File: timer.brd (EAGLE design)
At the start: 100 x 100 mm, 58 parts, among them IC1 CD4060, IC2 7805TV, K1 ZF112

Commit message: Added Values
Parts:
- C1: value (none) -> 100uF/16V
- C2: value (none) -> 0.3uF
- C3: value (none) -> 0.1uF
- C4: value (none) -> 100nF
- C5: value (none) -> 0.22uF
- JP1: value (none) -> 9V Battery
- JP2: value (none) -> Relay
- K1: value ZF112 -> 5V
- R1, R11, R20: value (none) -> 1K
- R12: value (none) -> 100K
- R15: value (none) -> 1M
- R16, R18: value (none) -> 10M
- R17: value (none) -> 22M
- R19: value (none) -> 3K
- S1: value DPDT_SEC -> DPDT Slide Switch
- S2: value MOMENTARY-SWITCH-SPST-PTH-6.0MM -> SPST Momentary Switch 6mm
- S3: value (none) -> DIP Switch
- S4: value (none) -> SPDT
- T1: value (none) -> BC547

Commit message: Values + OS Logo + Titlesheet
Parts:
- added LOGO1: OSHW-LOGOS-COPPER, SparkFun-Aesthetics:OSHW-LOGO-S_COPPER
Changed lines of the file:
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@@
 <layer number="112" name="tSilk" color="7" fill="1" visible="yes" active="yes"/>
 <layer number="113" name="IDFDebug" color="4" fill="1" visible="yes" active="yes"/>
+<layer number="114" name="Badge_Outline" color="7" fill="1" visible="no" active="yes"/>
+<layer number="115" name="ReferenceISLANDS" color="7" fill="1" visible="no" active="yes"/>
 <layer number="116" name="Patch_BOT" color="9" fill="4" visible="yes" active="yes"/>
 <layer number="118" name="Rect_Pads" color="7" fill="1" visible="yes" active="yes"/>
@@
 <attribute name="VALUE" x="73.75" y="78.722" size="1.27" layer="27" ratio="10" rot="R180"/>
 </element>
+<element name="LOGO1" library="SparkFun-Aesthetics" library_urn="urn:adsk.eagle:library:507" package="OSHW-LOGO-S_COPPER" value="OSHW-LOGOS-COPPER" x="119" y="15" smashed="yes"/>
 </elements>
 <signals>

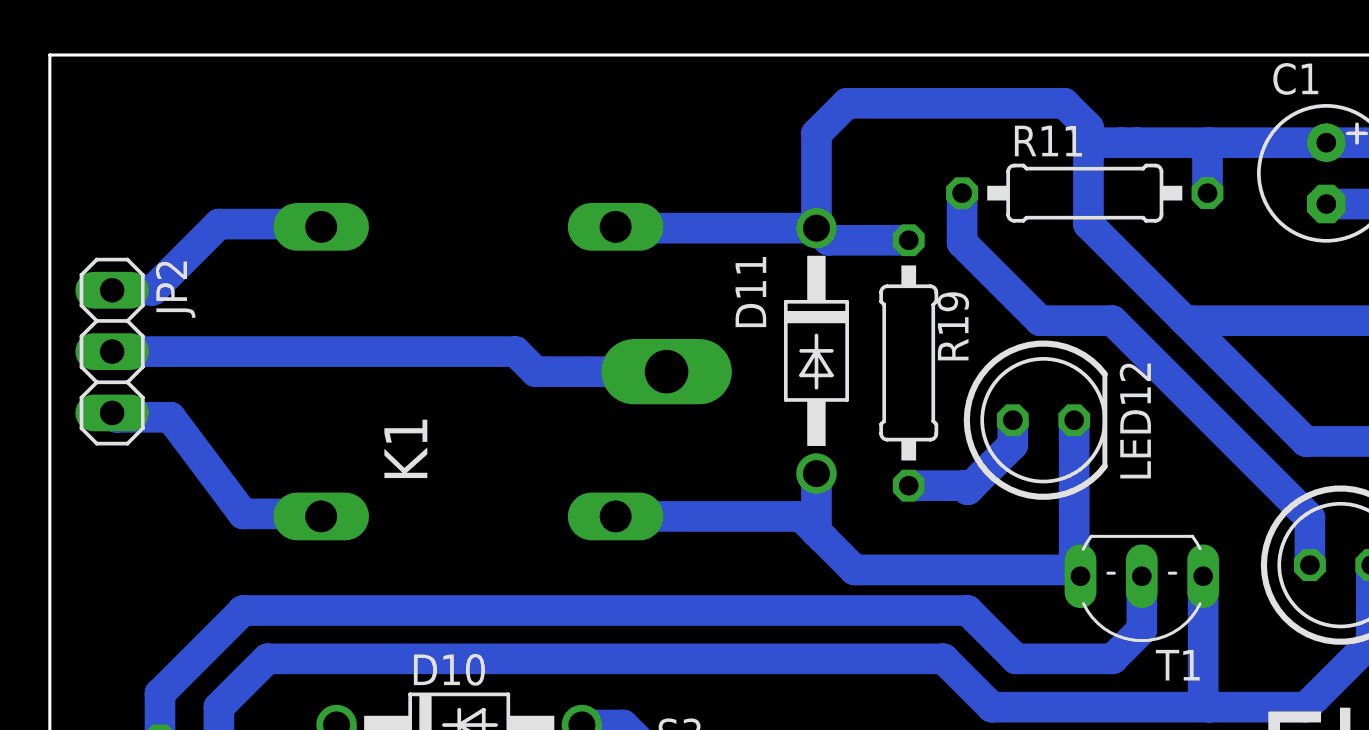
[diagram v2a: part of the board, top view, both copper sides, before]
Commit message: Changed Relay Output Connector
Pinhead JP2 changed to screw terminal J1
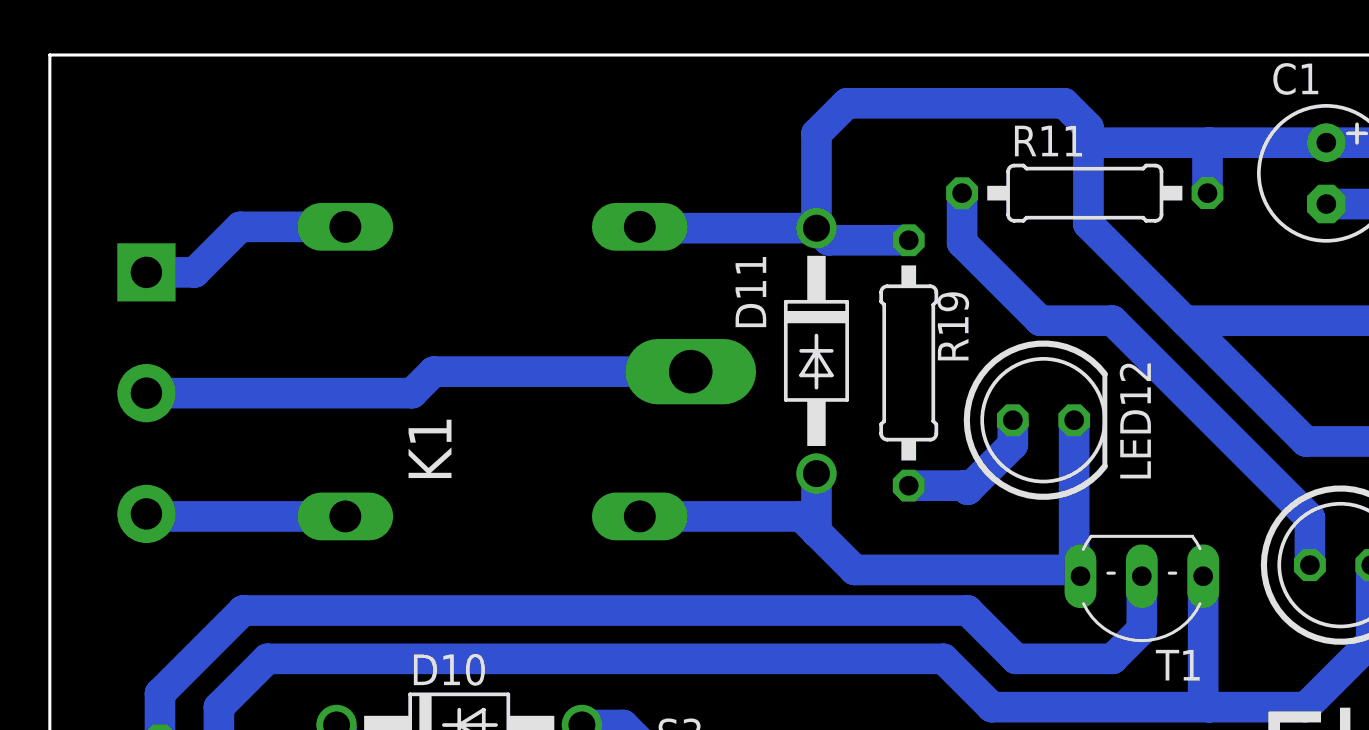
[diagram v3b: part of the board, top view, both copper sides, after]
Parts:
- removed JP2: Relay, pinhead:1X03
- added J1: Relay, SparkFun-Connectors:SCREWTERMINAL-5MM-3
- moved K1 1.00 mm to (44.3, 83.9)
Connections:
- net N$48: now also J1.2; no longer JP2.2
- net N$49: now also J1.3; no longer JP2.3
- net N$50: now also J1.1; no longer JP2.1
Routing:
- net N$49: track 10.8 -> 8.42 mm
- net N$45: track 28.9 -> 27.9 mm
- net 5V: track 140.5 -> 139.5 mm
- net N$50: track 9.84 -> 9.18 mm
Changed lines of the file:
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@@
 <layer number="230" name="230bmp" color="7" fill="1" visible="yes" active="yes"/>
 <layer number="231" name="231bmp" color="7" fill="1" visible="yes" active="yes"/>
+<layer number="232" name="Eagle3D_PG2" color="7" fill="1" visible="yes" active="yes"/>
+<layer number="233" name="Eagle3D_PG3" color="7" fill="1" visible="yes" active="yes"/>
 <layer number="248" name="Housing" color="7" fill="1" visible="yes" active="yes"/>
 <layer number="249" name="Edge" color="7" fill="1" visible="yes" active="yes"/>
@@
 <attribute name="VALUE" x="119.405" y="89.88" size="1.27" layer="27" rot="R270"/>
 </element>
-<element name="JP2" library="pinhead" library_urn="urn:adsk.eagle:library:325" package="1X03" package3d_urn="urn:adsk.eagle:package:22458/2" value="Relay" x="28.58" y="84.72" smashed="yes" rot="R270">
-<attribute name="NAME" x="30.4088" y="88.6062" size="1.27" layer="25" ratio="10" rot="R270"/>
-<attribute name="VALUE" x="30.405" y="84.53" size="1.27" layer="27" rot="R270"/>
-</element>
-<element name="K1" library="relay" library_urn="urn:adsk.eagle:library:339" package="ZF112" package3d_urn="urn:adsk.eagle:package:24315/1" value="5V" x="43.33" y="83.89" smashed="yes" rot="MR0">
-<attribute name="MF" value="" x="16.66" y="75" size="1.778" layer="28" rot="MR0" display="off"/>
-<attribute name="MPN" value="" x="16.66" y="75" size="1.778" layer="28" rot="MR0" display="off"/>
-<attribute name="NAME" x="41.63" y="79.27" size="1.778" layer="25" ratio="10" rot="R90"/>
-<attribute name="OC_FARNELL" value="unknown" x="16.66" y="75" size="1.778" layer="28" rot="MR0" display="off"/>
-<attribute name="OC_NEWARK" value="unknown" x="16.66" y="75" size="1.778" layer="28" rot="MR0" display="off"/>
+<element name="K1" library="relay" library_urn="urn:adsk.eagle:library:339" package="ZF112" package3d_urn="urn:adsk.eagle:package:24315/1" value="5V" x="44.33" y="83.89" smashed="yes" rot="MR0">
+<attribute name="MF" value="" x="17.66" y="75" size="1.778" layer="28" rot="MR0" display="off"/>
+<attribute name="MPN" value="" x="17.66" y="75" size="1.778" layer="28" rot="MR0" display="off"/>
+<attribute name="NAME" x="42.63" y="79.27" size="1.778" layer="25" ratio="10" rot="R90"/>
+<attribute name="OC_FARNELL" value="unknown" x="17.66" y="75" size="1.778" layer="28" rot="MR0" display="off"/>
+<attribute name="OC_NEWARK" value="unknown" x="17.66" y="75" size="1.778" layer="28" rot="MR0" display="off"/>
 </element>
 <element name="LED1" library="led" library_urn="urn:adsk.eagle:library:259" package="LED5MM" package3d_urn="urn:adsk.eagle:package:15799/2" value="" x="113.12" y="2.26" smashed="yes" rot="R270">
@@
 </element>
 <element name="LOGO1" library="SparkFun-Aesthetics" library_urn="urn:adsk.eagle:library:507" package="OSHW-LOGO-S_COPPER" value="OSHW-LOGOS-COPPER" x="119" y="15" smashed="yes"/>
+<element name="J1" library="SparkFun-Connectors" library_urn="urn:adsk.eagle:library:513" package="SCREWTERMINAL-5MM-3" value="Relay" x="30" y="88" smashed="yes" rot="MR270">
+<attribute name="NAME" x="27.206" y="84.317" size="0.6096" layer="26" font="vector" ratio="20" rot="MR270"/>
+<attribute name="PROD_ID" value="CONN-10134" x="30" y="88" size="1.778" layer="28" rot="MR270" display="off"/>
+<attribute name="SF_SKU" value="PRT-08433" x="30" y="88" size="1.778" layer="28" rot="MR270" display="off"/>
+<attribute name="VALUE" x="28.095" y="84.571" size="0.6096" layer="28" font="vector" ratio="20" rot="MR270"/>
+</element>
 </elements>
 <signals>
@@
 <contactref element="C4" pad="1"/>
 <wire x1="78.85" y1="93.37" x2="74" y2="93.37" width="1.27" layer="16"/>
-<wire x1="74" y1="93.37" x2="71" y2="93.37" width="1.27" layer="16"/>
-<wire x1="71" y1="93.37" x2="70.37" y2="93.37" width="1.27" layer="16"/>
+<wire x1="74" y1="93.37" x2="69.37" y2="93.37" width="1.27" layer="16"/>
 <wire x1="69" y1="90" x2="73" y2="86" width="1.27" layer="16"/>
 <wire x1="73" y1="86" x2="87" y2="86" width="1.27" layer="16"/>
@@
 <wire x1="61.56" y1="89.33" x2="58.24" y2="89.33" width="1.27" layer="16"/>
 <wire x1="58.24" y1="89.33" x2="57.74" y2="89.83" width="1.27" layer="16"/>
-<wire x1="57.74" y1="89.83" x2="49.4804" y2="89.83" width="1.27" layer="16"/>
-<wire x1="49.4804" y1="89.83" x2="49.426" y2="89.8844" width="1.27" layer="16"/>
+<wire x1="57.74" y1="89.83" x2="50.4804" y2="89.83" width="1.27" layer="16"/>
+<wire x1="50.4804" y1="89.83" x2="50.426" y2="89.8844" width="1.27" layer="16"/>
 <wire x1="57.74" y1="89.83" x2="57.74" y2="93.74" width="1.27" layer="16"/>
 <wire x1="57.74" y1="93.74" x2="59" y2="95" width="1.27" layer="16"/>
@@
 <wire x1="69" y1="93" x2="69" y2="90" width="1.27" layer="16"/>
 <wire x1="59" y1="95" x2="68" y2="95" width="1.27" layer="16"/>
-<wire x1="70.37" y1="93.37" x2="69.37" y2="93.37" width="1.27" layer="16"/>
 <wire x1="69.37" y1="93.37" x2="69" y2="93" width="1.27" layer="16"/>
 </signal>
@@
 <contactref element="D11" pad="A"/>
 <contactref element="K1" pad="2"/>
-<wire x1="49.426" y1="77.8956" x2="57.1044" y2="77.8956" width="1.27" layer="16"/>
+<wire x1="50.426" y1="77.8956" x2="57.1044" y2="77.8956" width="1.27" layer="16"/>
 <wire x1="57.1044" y1="77.8956" x2="57.74" y2="77.26" width="1.27" layer="16"/>
 <wire x1="57.74" y1="79.67" x2="57.74" y2="77.26" width="1.27" layer="16"/>
-<wire x1="57.74" y1="77.26" x2="58" y2="77" width="1.27" layer="16"/>
 <wire x1="68.41" y1="81.88" x2="68.41" y2="75.68" width="1.27" layer="16"/>
 <wire x1="68.41" y1="75.68" x2="68.67" y2="75.42" width="1.27" layer="16"/>
-<wire x1="58" y1="77" x2="59.32" y2="75.68" width="1.27" layer="16"/>
+<wire x1="57.74" y1="77.26" x2="59.32" y2="75.68" width="1.27" layer="16"/>
 <wire x1="59.32" y1="75.68" x2="68.41" y2="75.68" width="1.27" layer="16"/>
 </signal>
@@
 <signal name="N$48">
 <contactref element="K1" pad="P"/>
-<contactref element="JP2" pad="2"/>
-<wire x1="28.58" y1="84.72" x2="45.28" y2="84.72" width="1.27" layer="16"/>
-<wire x1="46.11" y1="83.89" x2="51.5342" y2="83.89" width="1.27" layer="16"/>
-<wire x1="45.28" y1="84.72" x2="46.11" y2="83.89" width="1.27" layer="16"/>
+<contactref element="J1" pad="2"/>
+<wire x1="52.5342" y1="83.89" x2="41.89" y2="83.89" width="1.27" layer="16"/>
+<wire x1="41.89" y1="83.89" x2="41" y2="83" width="1.27" layer="16"/>
+<wire x1="41" y1="83" x2="30" y2="83" width="1.27" layer="16"/>
 </signal>
 <signal name="N$49">
-<contactref element="JP2" pad="3"/>
 <contactref element="K1" pad="S"/>
-<wire x1="37.234" y1="77.8956" x2="37.1296" y2="78" width="1.27" layer="16"/>
-<wire x1="34" y1="78" x2="37.1296" y2="78" width="1.27" layer="16"/>
-<wire x1="28.58" y1="82.18" x2="28.76" y2="82" width="1.27" layer="16"/>
-<wire x1="28.76" y1="82" x2="31" y2="82" width="1.27" layer="16"/>
-<wire x1="31" y1="82" x2="34" y2="78" width="1.27" layer="16"/>
+<wire x1="38.234" y1="77.8956" x2="38.1296" y2="78" width="1.27" layer="16"/>
+<contactref element="J1" pad="3"/>
+<wire x1="38.234" y1="77.8956" x2="30.1044" y2="77.8956" width="1.27" layer="16"/>
+<wire x1="30.1044" y1="77.8956" x2="30" y2="78" width="1.27" layer="16"/>
 </signal>
 <signal name="N$50">
 <contactref element="K1" pad="O"/>
-<contactref element="JP2" pad="1"/>
-<wire x1="28.58" y1="87.26" x2="30.26" y2="87.26" width="1.27" layer="16"/>
-<wire x1="30.26" y1="87.26" x2="33" y2="90" width="1.27" layer="16"/>
-<wire x1="33" y1="90" x2="37.1184" y2="90" width="1.27" layer="16"/>
-<wire x1="37.1184" y1="90" x2="37.234" y2="89.8844" width="1.27" layer="16"/>
+<wire x1="38.1184" y1="90" x2="38.234" y2="89.8844" width="1.27" layer="16"/>
+<contactref element="J1" pad="1"/>
+<wire x1="38.234" y1="89.8844" x2="33.8844" y2="89.8844" width="1.27" layer="16"/>
+<wire x1="33.8844" y1="89.8844" x2="32" y2="88" width="1.27" layer="16"/>
+<wire x1="32" y1="88" x2="30" y2="88" width="1.27" layer="16"/>
 </signal>
 <signal name="N$51">

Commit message: Added values of R13,R14
910K Ohm
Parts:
- R13, R14: value (none) -> 910K
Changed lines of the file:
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@@
 <attribute name="VALUE" x="118.1106" y="67.355" size="1.27" layer="27" ratio="10" rot="R180"/>
 </element>
-<element name="R13" library="resistor" library_urn="urn:adsk.eagle:library:348" package="0207/10" package3d_urn="urn:adsk.eagle:package:23491/2" value="" x="117.64" y="29.05" smashed="yes" rot="R90">
+<element name="R13" library="resistor" library_urn="urn:adsk.eagle:library:348" package="0207/10" package3d_urn="urn:adsk.eagle:package:23491/2" value="910K" x="117.64" y="29.05" smashed="yes" rot="R90">
 <attribute name="NAME" x="116.116" y="26.002" size="1.27" layer="25" ratio="10" rot="R90"/>
 <attribute name="VALUE" x="118.275" y="26.7894" size="1.27" layer="27" ratio="10" rot="R90"/>
 </element>
-<element name="R14" library="resistor" library_urn="urn:adsk.eagle:library:348" package="0207/10" package3d_urn="urn:adsk.eagle:package:23491/2" value="" x="121.36" y="38.25" smashed="yes" rot="R270">
+<element name="R14" library="resistor" library_urn="urn:adsk.eagle:library:348" package="0207/10" package3d_urn="urn:adsk.eagle:package:23491/2" value="910K" x="121.36" y="38.25" smashed="yes" rot="R270">
 <attribute name="NAME" x="122.884" y="41.298" size="1.27" layer="25" ratio="10" rot="R270"/>
 <attribute name="VALUE" x="120.725" y="40.5106" size="1.27" layer="27" ratio="10" rot="R270"/>
